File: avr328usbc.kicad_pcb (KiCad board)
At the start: 2 copper layers, 73.3 x 45 mm, 23 parts, among them J1 USB-C THT, J2 MCP Debug Header, J3 USB-C THT, J4 Conn_01x14_MountingPin, J5 AVR-ISP-6, J6 Conn_01x14_MountingPin, J7 MCP Debug Header, U1 MCP2221AxP, U2 ACPL-772L-000E, U3 ACPL-772L-000E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

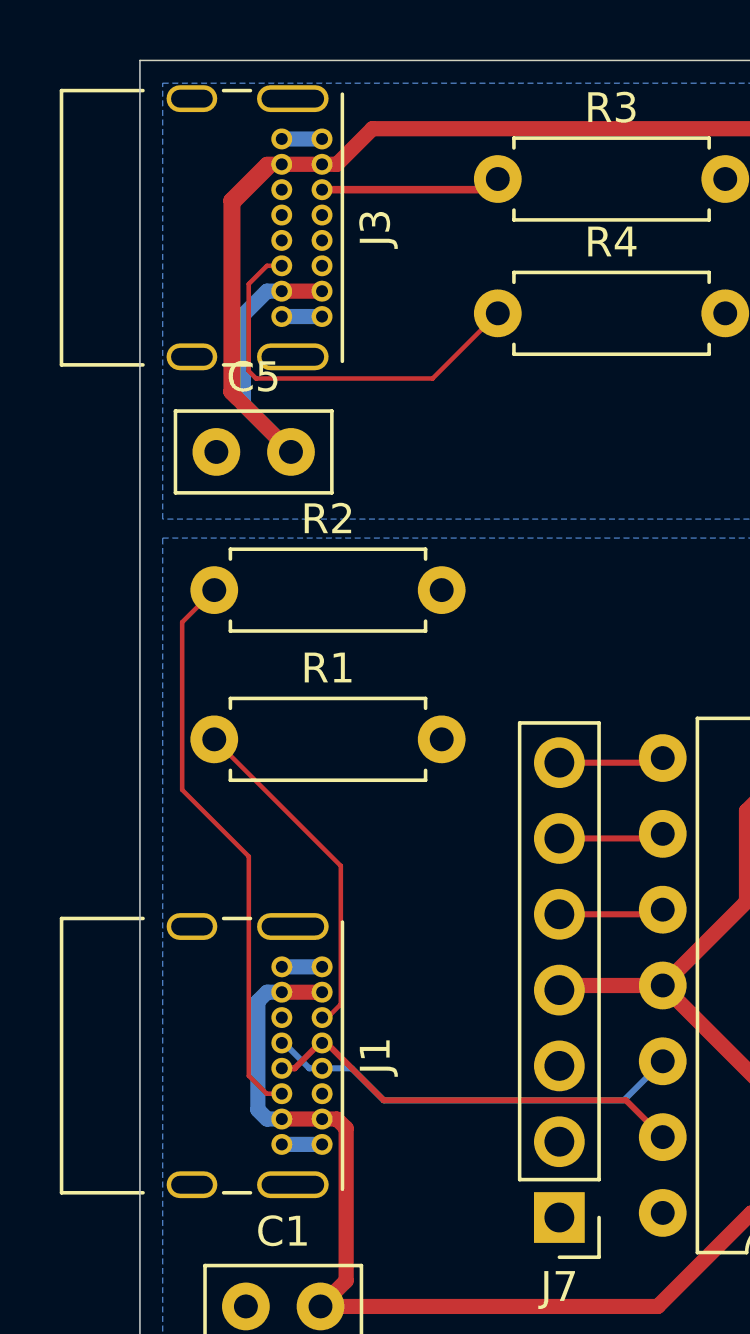
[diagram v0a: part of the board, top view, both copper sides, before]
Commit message: modified USB-C footprint to follow clearence rules at OSH
Now almost all DRCs pass
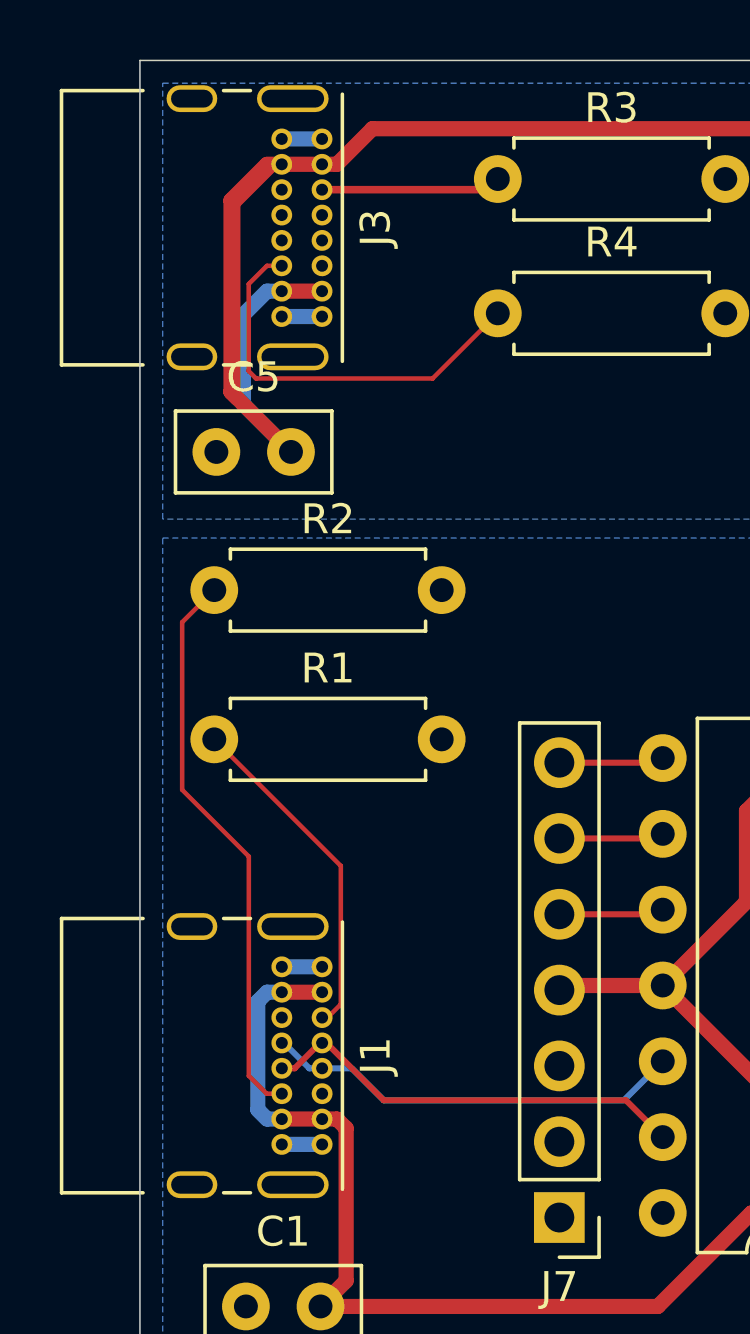
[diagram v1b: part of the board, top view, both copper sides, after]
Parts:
- J1, J3: footprint Connector_USB:USB_C_Receptacle_GCT_USB4085 -> AAAA_Project_Library:USB_C_Receptacle_GCT_USB4085_Reduced_Pad_Size
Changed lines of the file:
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@@
 		)
 	)
-	(footprint "Connector_USB:USB_C_Receptacle_GCT_USB4085"
-		(locked yes)
+	(footprint "AAAA_Project_Library:USB_C_Receptacle_GCT_USB4085_Reduced_Pad_Size"
 		(layer "F.Cu")
 		(at 82.301145 66.384274 -90)
@@
 		(tags "USB Type-C Receptacle Through-hole Right angle")
 		(property "Reference" "J3"
-			(at 2.975 -1.8 90)
+			(at 2.975 -1.8 -90)
 			(layer "F.SilkS")
 			(effects
@@
 		)
 		(property "Value" "USB-C THT"
-			(at 2.975 9.925 90)
+			(at 2.975 9.925 -90)
 			(layer "F.Fab")
 			(effects
@@
 			)
 		)
-		(property "Footprint" "Connector_USB:USB_C_Receptacle_GCT_USB4085"
+		(property "Footprint" "AAAA_Project_Library:USB_C_Receptacle_GCT_USB4085_Reduced_Pad_Size"
 			(at 0 0 -90)
 			(unlocked yes)
@@
 		)
 		(fp_text user "PCB Edge"
-			(at 2.975 6.1 90)
+			(at 2.975 6.1 -90)
 			(layer "Dwgs.User")
 			(effects
@@
 		)
 		(fp_text user "${REFERENCE}"
-			(at 2.975 4.025 90)
+			(at 2.975 4.025 -90)
 			(layer "F.Fab")
 			(effects
@@
 		(pad "A1" thru_hole circle
 			(at 0 0 270)
-			(size 0.7 0.7)
+			(size 0.69746 0.69746)
 			(drill 0.4)
 			(layers "*.Cu" "*.Mask")
@@
 		(pad "A4" thru_hole circle
 			(at 0.85 0 270)
-			(size 0.7 0.7)
+			(size 0.69746 0.69746)
 			(drill 0.4)
 			(layers "*.Cu" "*.Mask")
@@
 		(pad "A5" thru_hole circle
 			(at 1.7 0 270)
-			(size 0.7 0.7)
+			(size 0.69746 0.69746)
 			(drill 0.4)
 			(layers "*.Cu" "*.Mask")
@@
 		(pad "A6" thru_hole circle
 			(at 2.55 0 270)
-			(size 0.7 0.7)
+			(size 0.69746 0.69746)
 			(drill 0.4)
 			(layers "*.Cu" "*.Mask")
@@
 		(pad "A7" thru_hole circle
 			(at 3.4 0 270)
-			(size 0.7 0.7)
+			(size 0.69746 0.69746)
 			(drill 0.4)
 			(layers "*.Cu" "*.Mask")
@@
 		(pad "A8" thru_hole circle
 			(at 4.25 0 270)
-			(size 0.7 0.7)
+			(size 0.69746 0.69746)
 			(drill 0.4)
 			(layers "*.Cu" "*.Mask")
@@
 		(pad "A9" thru_hole circle
 			(at 5.1 0 270)
-			(size 0.7 0.7)
+			(size 0.69746 0.69746)
 			(drill 0.4)
 			(layers "*.Cu" "*.Mask")
@@
 		(pad "A12" thru_hole circle
 			(at 5.95 0 270)
-			(size 0.7 0.7)
+			(size 0.69746 0.69746)
 			(drill 0.4)
 			(layers "*.Cu" "*.Mask")
@@
 		(pad "B1" thru_hole circle
 			(at 5.95 1.35 270)
-			(size 0.7 0.7)
+			(size 0.69746 0.69746)
 			(drill 0.4)
 			(layers "*.Cu" "*.Mask")
@@
 		(pad "B4" thru_hole circle
 			(at 5.1 1.35 270)
-			(size 0.7 0.7)
+			(size 0.69746 0.69746)
 			(drill 0.4)
 			(layers "*.Cu" "*.Mask")
@@
 		(pad "B5" thru_hole circle
 			(at 4.25 1.35 270)
-			(size 0.7 0.7)
+			(size 0.69746 0.69746)
 			(drill 0.4)
 			(layers "*.Cu" "*.Mask")
@@
 		(pad "B6" thru_hole circle
 			(at 3.4 1.35 270)
-			(size 0.7 0.7)
+			(size 0.69746 0.69746)
 			(drill 0.4)
 			(layers "*.Cu" "*.Mask")
@@
 		(pad "B7" thru_hole circle
 			(at 2.55 1.35 270)
-			(size 0.7 0.7)
+			(size 0.69746 0.69746)
 			(drill 0.4)
 			(layers "*.Cu" "*.Mask")
@@
 		(pad "B8" thru_hole circle
 			(at 1.7 1.35 270)
-			(size 0.7 0.7)
+			(size 0.69746 0.69746)
 			(drill 0.4)
 			(layers "*.Cu" "*.Mask")
@@
 		(pad "B9" thru_hole circle
 			(at 0.85 1.35 270)
-			(size 0.7 0.7)
+			(size 0.69746 0.69746)
 			(drill 0.4)
 			(layers "*.Cu" "*.Mask")
@@
 		(pad "B12" thru_hole circle
 			(at 0 1.35 270)
-			(size 0.7 0.7)
+			(size 0.69746 0.69746)
 			(drill 0.4)
 			(layers "*.Cu" "*.Mask")
@@
 		)
 	)
-	(footprint "Connector_USB:USB_C_Receptacle_GCT_USB4085"
+	(footprint "AAAA_Project_Library:USB_C_Receptacle_GCT_USB4085_Reduced_Pad_Size"
 		(locked yes)
 		(layer "F.Cu")
@@
 		(tags "USB Type-C Receptacle Through-hole Right angle")
 		(property "Reference" "J1"
-			(at 2.975 -1.8 90)
+			(at 2.975 -1.8 -90)
 			(layer "F.SilkS")
 			(effects
@@
 		)
 		(property "Value" "USB-C THT"
-			(at 2.975 9.925 90)
+			(at 2.975 9.925 -90)
 			(layer "F.Fab")
 			(effects
@@
 			)
 		)
-		(property "Footprint" "Connector_USB:USB_C_Receptacle_GCT_USB4085"
+		(property "Footprint" "AAAA_Project_Library:USB_C_Receptacle_GCT_USB4085_Reduced_Pad_Size"
 			(at 0 0 -90)
 			(unlocked yes)
@@
 		)
 		(fp_text user "PCB Edge"
-			(at 2.975 6.1 90)
+			(at 2.975 6.1 -90)
 			(layer "Dwgs.User")
 			(effects
@@
 		)
 		(fp_text user "${REFERENCE}"
-			(at 2.975 4.025 90)
+			(at 2.975 4.025 -90)
 			(layer "F.Fab")
 			(effects
@@
 		(pad "A1" thru_hole circle
 			(at 0 0 270)
-			(size 0.7 0.7)
+			(size 0.69746 0.69746)
 			(drill 0.4)
 			(layers "*.Cu" "*.Mask")
@@
 		(pad "A4" thru_hole circle
 			(at 0.85 0 270)
-			(size 0.7 0.7)
+			(size 0.69746 0.69746)
 			(drill 0.4)
 			(layers "*.Cu" "*.Mask")
@@
 		(pad "A5" thru_hole circle
 			(at 1.7 0 270)
-			(size 0.7 0.7)
+			(size 0.69746 0.69746)
 			(drill 0.4)
 			(layers "*.Cu" "*.Mask")
@@
 		(pad "A6" thru_hole circle
 			(at 2.55 0 270)
-			(size 0.7 0.7)
+			(size 0.69746 0.69746)
 			(drill 0.4)
 			(layers "*.Cu" "*.Mask")
@@
 		(pad "A7" thru_hole circle
 			(at 3.4 0 270)
-			(size 0.7 0.7)
+			(size 0.69746 0.69746)
 			(drill 0.4)
 			(layers "*.Cu" "*.Mask")
@@
 		(pad "A8" thru_hole circle
 			(at 4.25 0 270)
-			(size 0.7 0.7)
+			(size 0.69746 0.69746)
 			(drill 0.4)
 			(layers "*.Cu" "*.Mask")
@@
 		(pad "A9" thru_hole circle
 			(at 5.1 0 270)
-			(size 0.7 0.7)
+			(size 0.69746 0.69746)
 			(drill 0.4)
 			(layers "*.Cu" "*.Mask")
@@
 		(pad "A12" thru_hole circle
 			(at 5.95 0 270)
-			(size 0.7 0.7)
+			(size 0.69746 0.69746)
 			(drill 0.4)
 			(layers "*.Cu" "*.Mask")
@@
 		(pad "B1" thru_hole circle
 			(at 5.95 1.35 270)
-			(size 0.7 0.7)
+			(size 0.69746 0.69746)
 			(drill 0.4)
 			(layers "*.Cu" "*.Mask")
@@
 		(pad "B4" thru_hole circle
 			(at 5.1 1.35 270)
-			(size 0.7 0.7)
+			(size 0.69746 0.69746)
 			(drill 0.4)
 			(layers "*.Cu" "*.Mask")
@@
 		(pad "B5" thru_hole circle
 			(at 4.25 1.35 270)
-			(size 0.7 0.7)
+			(size 0.69746 0.69746)
 			(drill 0.4)
 			(layers "*.Cu" "*.Mask")
@@
 		(pad "B6" thru_hole circle
 			(at 3.4 1.35 270)
-			(size 0.7 0.7)
+			(size 0.69746 0.69746)
 			(drill 0.4)
 			(layers "*.Cu" "*.Mask")
@@
 		(pad "B7" thru_hole circle
 			(at 2.55 1.35 270)
-			(size 0.7 0.7)
+			(size 0.69746 0.69746)
 			(drill 0.4)
 			(layers "*.Cu" "*.Mask")
@@
 		(pad "B8" thru_hole circle
 			(at 1.7 1.35 270)
-			(size 0.7 0.7)
+			(size 0.69746 0.69746)
 			(drill 0.4)
 			(layers "*.Cu" "*.Mask")
@@
 		(pad "B9" thru_hole circle
 			(at 0.85 1.35 270)
-			(size 0.7 0.7)
+			(size 0.69746 0.69746)
 			(drill 0.4)
 			(layers "*.Cu" "*.Mask")
@@
 		(pad "B12" thru_hole circle
 			(at 0 1.35 270)
-			(size 0.7 0.7)
+			(size 0.69746 0.69746)
 			(drill 0.4)
 			(layers "*.Cu" "*.Mask")
